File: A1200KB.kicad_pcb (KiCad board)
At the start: 2 copper layers, 453 x 140 mm, 112 parts, among them J1 Conn_01x32_Female, K1 ESC, K10 F9, K11 F10, K12 TILDE, K13 1, K14 2, K15 3, K16 4, K17 5, K18 6, K19 7, K2 F1, K20 8, K21 9, K22 0, K23 MINUS, K24 PLUS, K25 PIPE, K26 BS, K27 DEL, K28 HELP, K29 NUM_(, K3 F2, K30 NUM_), K31 NUM_DIV, K32 NUM_MULT, K33 TAB, K34 Q, K35 W, K36 E, K37 R, K38 T, K39 Y, K4 F3, K40 U, K41 I, K42 O, K43 P, K44 L.CURLY, K45 R.CURLY, K46 RETURN, K47 NUM_7, K48 NUM_8, K49 NUM_9, K5 F4, K50 NUM_MINUS, K51 CTRL, K52 CAPSLOCK, K53 A, K54 S, K55 D, K56 F, K57 G, K58 H, K59 J, K6 F5, K60 K, K61 L, K62 COLON, K63 ", K64 R.BLANK, K65 UP, K66 NUM_4, K67 NUM_5, K68 NUM_6, K69 NUM_PLUS, K7 F6, K70 L.SHIFT, K71 L.BLANK, K72 Z, K73 X, K74 C, K75 V, K76 B, K77 N, K78 M, K79 R.CROC, K8 F7, K80 L.CROC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

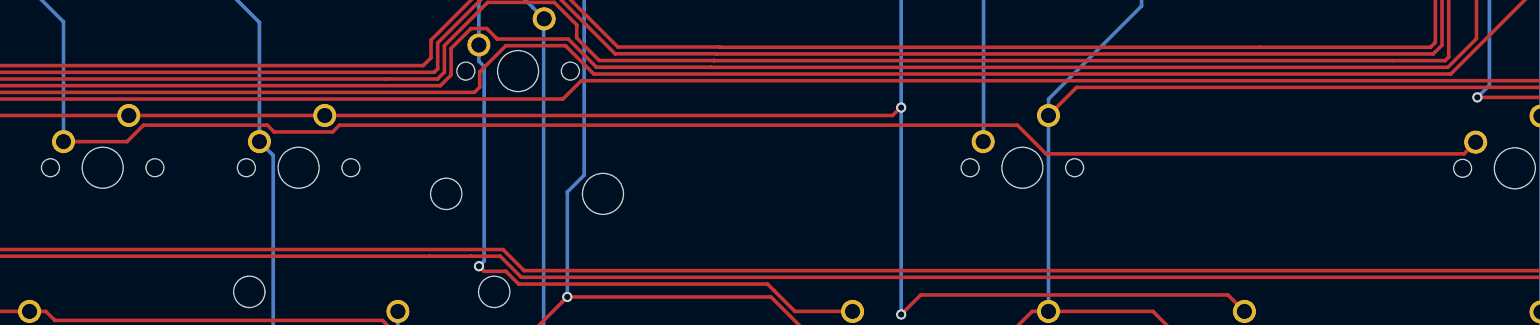
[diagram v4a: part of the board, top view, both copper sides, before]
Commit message: fixed bad route at return key
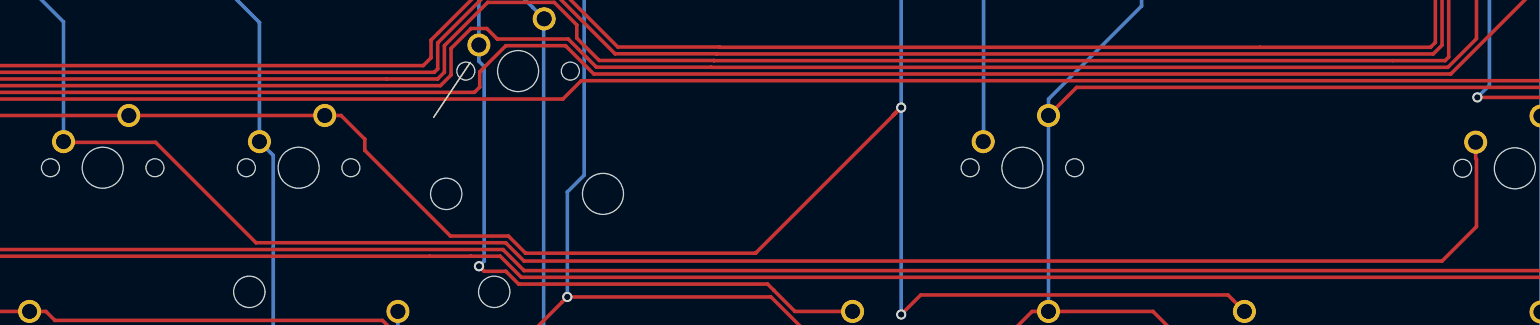
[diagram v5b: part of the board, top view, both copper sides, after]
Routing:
- net /2: track 535.5 -> 548.4 mm
- net /26: track 285.0 -> 296.7 mm
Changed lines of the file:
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@@
-(kicad_pcb (version 20171130) (host pcbnew "(5.1.0-0)")
+(kicad_pcb (version 20171130) (host pcbnew "(5.1.4-0-10_14)")
   (general
     (thickness 2)
-    (drawings 13)
-    (tracks 1275)
+    (drawings 14)
+    (tracks 1281)
     (zones 0)
     (modules 112)
@@
     (add_net "Net-(K46-Pad4)")
   )
+  (module MX_Alps_Hybrid:MXOnly-1U-NoLED (layer F.Cu)
+    (at 397.726 103.252)
+    (fp_text reference K66 (at 0 3.175) (layer Dwgs.User)
+      (effects (font (size 1 1) (thickness 0.15)))
+    )
+    (fp_text value NUM_4 (at 0 -7.9375) (layer Dwgs.User)
+      (effects (font (size 1 1) (thickness 0.15)))
+    )
+    (fp_line (start 5 -7) (end 7 -7) (layer Dwgs.User) (width 0.15))
+    (fp_line (start 7 -7) (end 7 -5) (layer Dwgs.User) (width 0.15))
+    (fp_line (start 5 7) (end 7 7) (layer Dwgs.User) (width 0.15))
+    (fp_line (start 7 7) (end 7 5) (layer Dwgs.User) (width 0.15))
+    (fp_line (start -7 5) (end -7 7) (layer Dwgs.User) (width 0.15))
+    (fp_line (start -7 7) (end -5 7) (layer Dwgs.User) (width 0.15))
+    (fp_line (start -5 -7) (end -7 -7) (layer Dwgs.User) (width 0.15))
+    (fp_line (start -7 -7) (end -7 -5) (layer Dwgs.User) (width 0.15))
+    (fp_line (start -9.525 -9.525) (end 9.525 -9.525) (layer Dwgs.User) (width 0.15))
+    (fp_line (start 9.525 -9.525) (end 9.525 9.525) (layer Dwgs.User) (width 0.15))
+    (fp_line (start 9.525 9.525) (end -9.525 9.525) (layer Dwgs.User) (width 0.15))
+    (fp_line (start -9.525 9.525) (end -9.525 -9.525) (layer Dwgs.User) (width 0.15))
+    (pad 2 thru_hole circle (at 2.54 -5.08) (size 2.25 2.25) (drill 1.47) (layers *.Cu B.Mask)
+      (net 26 /4))
+    (pad "" np_thru_hole circle (at 0 0) (size 3.9878 3.9878) (drill 3.9878) (layers *.Cu *.Mask))
+    (pad 1 thru_hole circle (at -3.81 -2.54) (size 2.25 2.25) (drill 1.47) (layers *.Cu B.Mask)
+      (net 10 /26))
+    (pad "" np_thru_hole circle (at -5.08 0 48.0996) (size 1.75 1.75) (drill 1.75) (layers *.Cu *.Mask))
+    (pad "" np_thru_hole circle (at 5.08 0 48.0996) (size 1.75 1.75) (drill 1.75) (layers *.Cu *.Mask))
+  )
   (module MX_Alps_Hybrid:MXOnly-1.25U-NoLED (layer F.Cu)
     (at 186.006 36.844)
@@
   )
   (module MX_Alps_Hybrid:MXOnly-1U-NoLED (layer F.Cu)
-    (at 397.726 103.252)
-    (fp_text reference K66 (at 0 3.175) (layer Dwgs.User)
-      (effects (font (size 1 1) (thickness 0.15)))
-    )
-    (fp_text value NUM_4 (at 0 -7.9375) (layer Dwgs.User)
-      (effects (font (size 1 1) (thickness 0.15)))
-    )
-    (fp_line (start 5 -7) (end 7 -7) (layer Dwgs.User) (width 0.15))
-    (fp_line (start 7 -7) (end 7 -5) (layer Dwgs.User) (width 0.15))
-    (fp_line (start 5 7) (end 7 7) (layer Dwgs.User) (width 0.15))
-    (fp_line (start 7 7) (end 7 5) (layer Dwgs.User) (width 0.15))
-    (fp_line (start -7 5) (end -7 7) (layer Dwgs.User) (width 0.15))
-    (fp_line (start -7 7) (end -5 7) (layer Dwgs.User) (width 0.15))
-    (fp_line (start -5 -7) (end -7 -7) (layer Dwgs.User) (width 0.15))
-    (fp_line (start -7 -7) (end -7 -5) (layer Dwgs.User) (width 0.15))
-    (fp_line (start -9.525 -9.525) (end 9.525 -9.525) (layer Dwgs.User) (width 0.15))
-    (fp_line (start 9.525 -9.525) (end 9.525 9.525) (layer Dwgs.User) (width 0.15))
-    (fp_line (start 9.525 9.525) (end -9.525 9.525) (layer Dwgs.User) (width 0.15))
-    (fp_line (start -9.525 9.525) (end -9.525 -9.525) (layer Dwgs.User) (width 0.15))
-    (pad 2 thru_hole circle (at 2.54 -5.08) (size 2.25 2.25) (drill 1.47) (layers *.Cu B.Mask)
-      (net 26 /4))
-    (pad "" np_thru_hole circle (at 0 0) (size 3.9878 3.9878) (drill 3.9878) (layers *.Cu *.Mask))
-    (pad 1 thru_hole circle (at -3.81 -2.54) (size 2.25 2.25) (drill 1.47) (layers *.Cu B.Mask)
-      (net 10 /26))
-    (pad "" np_thru_hole circle (at -5.08 0 48.0996) (size 1.75 1.75) (drill 1.75) (layers *.Cu *.Mask))
-    (pad "" np_thru_hole circle (at 5.08 0 48.0996) (size 1.75 1.75) (drill 1.75) (layers *.Cu *.Mask))
-  )
-  (module MX_Alps_Hybrid:MXOnly-1U-NoLED (layer F.Cu)
     (at 416.776 103.252)
     (fp_text reference K67 (at 0 3.175) (layer Dwgs.User)
@@
       (net 12 /28))
   )
+  (gr_line (start 296.164 92.964) (end 292.608 98.298) (layer F.SilkS) (width 0.15))
   (gr_line (start 422 19) (end 464 19) (layer Edge.Cuts) (width 0.15))
   (gr_line (start 422 19) (end 422 51) (layer Edge.Cuts) (width 0.15))
@@
   (segment (start 252.879099 85.269099) (end 256.618 89.008) (width 0.35) (layer B.Cu) (net 10))
   (segment (start 251.538 81.608) (end 251.538 83.19899) (width 0.35) (layer B.Cu) (net 10))
-  (segment (start 258.20899 100.658) (end 256.618 100.658) (width 0.35) (layer F.Cu) (net 10))
-  (segment (start 264.396003 99.057999) (end 262.796002 100.658) (width 0.35) (layer F.Cu) (net 10))
-  (segment (start 283.446003 99.057999) (end 282.786001 99.718001) (width 0.35) (layer F.Cu) (net 10))
-  (segment (start 349.357973 99.057999) (end 283.446003 99.057999) (width 0.35) (layer F.Cu) (net 10))
-  (segment (start 262.796002 100.658) (end 258.20899 100.658) (width 0.35) (layer F.Cu) (net 10))
-  (segment (start 352.147973 101.847999) (end 349.357973 99.057999) (width 0.35) (layer F.Cu) (net 10))
-  (segment (start 276.436001 99.057999) (end 264.396003 99.057999) (width 0.35) (layer F.Cu) (net 10))
-  (segment (start 277.096003 99.718001) (end 276.436001 99.057999) (width 0.35) (layer F.Cu) (net 10))
-  (segment (start 282.786001 99.718001) (end 277.096003 99.718001) (width 0.35) (layer F.Cu) (net 10))
-  (segment (start 392.780001 101.847999) (end 352.147973 101.847999) (width 0.35) (layer F.Cu) (net 10))
-  (segment (start 393.916 100.712) (end 392.780001 101.847999) (width 0.35) (layer F.Cu) (net 10))
   (segment (start 181.41 49.309238) (end 181.4 49.299238) (width 0.35) (layer B.Cu) (net 10))
   (segment (start 181.41 52.39) (end 181.41 49.309238) (width 0.35) (layer B.Cu) (net 10))
@@
   (segment (start 186.36 42.07) (end 181.4 42.07) (width 0.35) (layer F.Cu) (net 10))
   (segment (start 229.948 34.304) (end 223.535252 34.304) (width 0.35) (layer F.Cu) (net 10))
+  (segment (start 265.575099 100.729099) (end 275.336 110.49) (width 0.35) (layer F.Cu) (net 10))
+  (segment (start 256.689099 100.729099) (end 265.575099 100.729099) (width 0.35) (layer F.Cu) (net 10))
+  (segment (start 256.618 100.658) (end 256.689099 100.729099) (width 0.35) (layer F.Cu) (net 10))
+  (segment (start 275.336 110.49) (end 299.607756 110.49) (width 0.35) (layer F.Cu) (net 10))
+  (segment (start 299.607756 110.49) (end 301.385756 112.268) (width 0.35) (layer F.Cu) (net 10))
+  (segment (start 301.385756 112.268) (end 390.652 112.268) (width 0.35) (layer F.Cu) (net 10))
+  (segment (start 393.916 102.30299) (end 393.916 100.712) (width 0.35) (layer F.Cu) (net 10))
+  (segment (start 393.996001 102.382991) (end 393.916 102.30299) (width 0.35) (layer F.Cu) (net 10))
+  (segment (start 393.996001 108.923999) (end 393.996001 102.382991) (width 0.35) (layer F.Cu) (net 10))
+  (segment (start 390.652 112.268) (end 393.996001 108.923999) (width 0.35) (layer F.Cu) (net 10))
   (segment (start 261.19 41.839828) (end 261.19 62.558) (width 0.35) (layer B.Cu) (net 11))
   (segment (start 258.819073 39.468901) (end 261.19 41.839828) (width 0.35) (layer B.Cu) (net 11))
@@
   (segment (start 369.833999 115.567999) (end 370.309001 116.043001) (width 0.35) (layer F.Cu) (net 22))
   (segment (start 338.062 117.468) (end 339.962001 115.567999) (width 0.35) (layer F.Cu) (net 22))
-  (segment (start 282.018 98.118) (end 337.232 98.118) (width 0.35) (layer F.Cu) (net 22))
   (segment (start 337.232 98.118) (end 338.02 97.33) (width 0.35) (layer F.Cu) (net 22))
   (segment (start 338.062 97.348) (end 338.062 117.468) (width 0.35) (layer B.Cu) (net 22))
   (via (at 338.062 97.348) (size 1) (drill 0.6) (layers F.Cu B.Cu) (net 22))
+  (segment (start 323.904 111.506) (end 338.062 97.348) (width 0.35) (layer F.Cu) (net 22))
+  (segment (start 299.876998 109.83999) (end 301.543008 111.506) (width 0.35) (layer F.Cu) (net 22))
+  (segment (start 285.908001 101.504001) (end 294.24399 109.83999) (width 0.35) (layer F.Cu) (net 22))
+  (segment (start 285.908001 100.417011) (end 285.908001 101.504001) (width 0.35) (layer F.Cu) (net 22))
+  (segment (start 301.543008 111.506) (end 323.904 111.506) (width 0.35) (layer F.Cu) (net 22))
+  (segment (start 283.60899 98.118) (end 285.908001 100.417011) (width 0.35) (layer F.Cu) (net 22))
+  (segment (start 294.24399 109.83999) (end 299.876998 109.83999) (width 0.35) (layer F.Cu) (net 22))
+  (segment (start 282.018 98.118) (end 283.60899 98.118) (width 0.35) (layer F.Cu) (net 22))
   (segment (start 149.077769 47.352979) (end 149.077767 47.352981) (width 0.35) (layer F.Cu) (net 23))
   (segment (start 160.122979 47.352979) (end 149.077769 47.352979) (width 0.35) (layer F.Cu) (net 23))

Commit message: Rev 3!
Board is smaller for more flexibility in mounting. Stabs are turned inwards. Traces moved to make fitting mounting holes easier. This will need a new 3D printed mounting solution…
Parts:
- removed the REF** at (213.3, 152.7)
- removed the REF** at (467.1, 152.0)
- removed the REF** at (65.6, 152.0)
- removed the REF** at (23.8, 151.9)
- removed the REF** at (16.8, 112.5)
- removed the REF** at (17.4, 52.4)
- removed the REF** at (129.2, 18.2)
- removed the REF** at (53.4, 16.8)
- removed the REF** at (419.0, 19.3)
- removed the REF** at (327.1, 18.4)
- removed the REF** at (226.7, 18.7)
- removed the REF** at (470.5, 103.9)
- removed the REF** at (470.5, 66.2)
- removed the REF** at (467.3, 151.8)
- added BK1: BLANK, MX_Alps_Hybrid:MXOnly-1U-NoLED, F.Cu at (86.7, 141.3)
- added BK2: BLANK, MX_Alps_Hybrid:MXOnly-1U-NoLED, F.Cu at (239.1, 141.3)
- added REF**: MountingHole_3.2mm_M3, MountingHole:MountingHole_3.2mm_M3, F.Cu at (385.4, 141.7)
- added REF**: MountingHole_3.2mm_M3, MountingHole:MountingHole_3.2mm_M3, F.Cu at (457.7, 113.8)
- added REF**: MountingHole_3.2mm_M3, MountingHole:MountingHole_3.2mm_M3, F.Cu at (310.4, 141.9)
- added REF**: MountingHole_3.2mm_M3, MountingHole:MountingHole_3.2mm_M3, F.Cu at (210.6, 141.7)
- added REF**: MountingHole_3.2mm_M3, MountingHole:MountingHole_3.2mm_M3, F.Cu at (110.5, 141.7)
- added REF**: MountingHole_3.2mm_M3, MountingHole:MountingHole_3.2mm_M3, F.Cu at (22.5, 141.9)
- added REF**: MountingHole_3.2mm_M3, MountingHole:MountingHole_3.2mm_M3, F.Cu at (22.5, 51.8)
- moved J1 1.50 mm to (167.4, 51.1)
- moved K1 1.50 mm to (25.5, 37.1)
- moved K10 1.50 mm to (256.1, 36.8)
- moved K11 1.50 mm to (280.0, 36.8)
- moved K12 1.50 mm to (30.2, 65.1)
- moved K13 1.50 mm to (54.0, 65.1)
- moved K14 1.50 mm to (73.0, 65.1)
- moved K15 1.50 mm to (92.0, 65.1)
- moved K16 1.50 mm to (111.1, 65.1)
- moved K17 1.50 mm to (130.2, 65.1)
- moved K18 1.50 mm to (149.2, 65.1)
- moved K19 1.50 mm to (168.2, 65.1)
- moved K2 1.50 mm to (56.5, 37.1)
- moved K20 1.50 mm to (187.3, 65.1)
- moved K21 1.50 mm to (206.3, 65.1)
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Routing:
- net /31: track 270.6 -> 216.3 mm, vias 0 -> 1
- net /9: track 223.5 -> 180.4 mm, vias 0 -> 1
- net /4: track 575.8 -> 598.3 mm
- net /20: track 457.7 -> 476.7 mm
- net /15: track 620.3 -> 634.3 mm
- net /3: track 542.6 -> 556.4 mm
- net /29: track 411.8 -> 423.4 mm
- net /11: track 195.4 -> 184.1 mm
- net /30: track 473.5 -> 462.4 mm
- net /7: track 445.5 -> 456.0 mm
- net /17: track 584.9 -> 594.1 mm
- net /19: track 508.0 -> 515.6 mm
- net /24: track 433.4 -> 440.6 mm
- net /12: track 214.4 -> 207.6 mm
- net /1: track 492.1 -> 488.1 mm
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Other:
- board size 453 x 140 mm -> 449.2 x 124.3 mm
- board text added: "195, 115"
- board text added: "295, 115"
- board text added: "370, 115"
- board text added: "442, 87"
- board text added: "7, 115"
- board text added: "7, 25"
- board text added: "95, 115"
- board text added: "December 2019"
- board text added: "Rev.3"
- board text removed: "Rev.2"
- board text removed: "april 2019"

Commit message: Better alignment of key groups with each other
More or less a perfect fit now. Also new mount STLs for A1200.net case. I'm getting around to redoing the Commodore case mounts soon.
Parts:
- removed BK1, BK2: BLANK, MX_Alps_Hybrid:MXOnly-1U-NoLED
- removed the REF** at (385.4, 141.7)
- removed the REF** at (457.7, 113.8)
- removed the REF** at (310.4, 141.9)
- removed the REF** at (210.6, 141.7)
- removed the REF** at (110.5, 141.7)
- added REF**: MountingHole_3.2mm_M3, MountingHole:MountingHole_3.2mm_M3, F.Cu at (465.4, 137.0)
- moved K38 60.5 mm to (174.9, 133.3)
- moved K34 60.5 mm to (98.7, 133.2)
- moved K35 60.5 mm to (117.8, 133.2)
- moved K36 60.5 mm to (136.8, 133.2)
- moved K37 60.5 mm to (155.9, 133.2)
- moved K42 60.5 mm to (251.1, 133.2)
- moved K43 60.5 mm to (270.2, 133.2)
- moved K33 60.5 mm to (70.3, 133.2)
- moved K39 60.5 mm to (194.0, 133.2)
- moved K40 60.5 mm to (213.0, 133.2)
- moved K41 60.5 mm to (232.1, 133.2)
- moved K12 60.5 mm to (65.5, 114.2)
- moved K14 60.5 mm to (108.4, 114.2)
- moved K15 60.5 mm to (127.4, 114.2)
- moved K18 60.5 mm to (184.6, 114.2)
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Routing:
- net /2: track 549.9 -> 427.2 mm, vias 3 -> 2
- net /1: track 488.1 -> 384.6 mm, vias 3 -> 2
- net /15: track 634.3 -> 551.7 mm
- net /17: track 594.1 -> 514.7 mm, vias 1 -> 3
- net /3: track 556.4 -> 493.1 mm
- net /21: track 388.1 -> 446.5 mm, vias 3 -> 7
- net /18: track 538.4 -> 483.4 mm, vias 1 -> 3
- net /5: track 371.4 -> 405.5 mm, vias 2 -> 3
- net /31: track 216.3 -> 243.0 mm, vias 1 -> 2
- net /6: track 202.4 -> 178.0 mm
- net /20: track 476.7 -> 453.8 mm
- net /13: track 219.5 -> 241.4 mm
- net /23: track 338.7 -> 359.7 mm, vias 1 -> 2
- net /24: track 440.6 -> 421.4 mm, vias 1 -> 3
- net /25: track 320.5 -> 301.4 mm
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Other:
- board size 449.2 x 124.3 mm -> 450 x 125 mm
- board text added: "+"
- board text added: "7,103"
- board text added: "7,38"
- board text added: "7,7"
- board text added: "July 2021"
- board text added: "Rev.4"
- board text removed: "195, 115"
- board text removed: "295, 115"
- board text removed: "370, 115"
- board text removed: "442, 87"
- board text removed: "7, 115"
- board text removed: "7, 25"
- board text removed: "95, 115"
- board text removed: "December 2019"
- board text removed: "Rev.3"
